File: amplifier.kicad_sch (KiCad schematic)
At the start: 16 parts, among them J1 Conn_01x01, J2 Conn_01x01, U2 IR2104, U5 IR2104

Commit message: Seems reasonable
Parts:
- removed C1, C9: C, symbol Device:C
- removed J1, J2: Conn_01x01, symbol Connector_Generic:Conn_01x01
- removed U10, U8: ~, symbol custom_symbols:NX3008N
- removed U2, U5: IR2104, Package_SO:SOIC-8_3.9x4.9mm_P1.27mm, symbol Driver_FET:IR2104
- added C11, C14, C15, C17, C4, C6: 10u, Capacitor_SMD:C_0603_1608Metric, symbol Device:C
- added Q1, Q2, Q3, Q4: DMN6140, Package_TO_SOT_SMD:SOT-23, symbol Transistor_FET:2N7002
- added R1, R11: 2k, Resistor_SMD:R_0603_1608Metric, symbol Device:R
- added TP2: LHI, TestPoint:TestPoint_Pad_D1.0mm, symbol Connector:TestPoint
- added TP4: LLO, TestPoint:TestPoint_Pad_D1.0mm, symbol Connector:TestPoint
- added TP6: RLO, TestPoint:TestPoint_Pad_D1.0mm, symbol Connector:TestPoint
- added TP7: RHI, TestPoint:TestPoint_Pad_D1.0mm, symbol Connector:TestPoint
- added U3: MIC4606, Package_SO:TSSOP-16-1EP_4.4x5mm_P0.65mm, symbol custom_symbols:MIC4606
- C10, C7, C8: value C -> 10u; footprint (none) -> Capacitor_SMD:C_0603_1608Metric
- R3, R5, R7, R9: value 100k -> 2k; footprint (none) -> Resistor_SMD:R_0603_1608Metric
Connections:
- net GND: now also C11.2, C14.2, C15.2, C17.2, C6.2, Q2.2 (S), Q4.2 (S), U3.13 (VSS)
- net OUT_A: now also C6.1, Q1.2 (S), Q2.3 (D), U3.15 (BHS); no longer C7.1, C8.1
- net OUT_B: now also C8.1, C4.2, Q3.2 (S), Q4.3 (D), U3.10 (AHS)
- net SIG_IN: now also R1.2
- net Vdrive: now also C7.1, C11.1, C14.1, Q1.3 (D), Q3.3 (D), U3.12 (VDD), U3.2 (EN); no longer C10.1
- net ~{SIG_IN}: now also R11.2
- net L_HI: now reaches R5.2
- net L_HI: now also TP2.1, U3.16 (BHO)
- net R_HI: now reaches R7.1
- net R_HI: now also TP7.1, U3.9 (AHO)
- net R_LO: now reaches R9.1
- net R_LO: now also TP6.1, U3.11 (ALO)
- net at R9.2: now also Q4.1 (G)
- net at R5.1: now also Q1.1 (G)
- net L_LO: now reaches R3.2
- net L_LO: now also TP4.1, U3.14 (BLO)
- net at R7.2: now also Q3.1 (G)
- net at R3.1: now also Q2.1 (G)
- new net: C10.1, U3.1 (BHB)
- new net: C17.1, R1.1, U3.3 (BPWM)
- new net: C15.1, R11.1, U3.6 (APWM)
- new net: C4.1, U3.8 (AHB)

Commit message: Tweaks
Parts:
- removed C6, C8: 10u, Capacitor_SMD:C_0603_1608Metric, symbol Device:C
- added C5: 2.2n, Capacitor_SMD:C_0603_1608Metric, symbol Device:C
- added L2: 10u, Inductor_SMD:L_1210_3225Metric, symbol Device:L
- C15, C17: value 10u -> 2.2n
- OUT1: now left out of the parts list
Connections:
- net GND: now also L2.2
- net OUT_A: now also C5.1
- new net: C5.2, L2.1
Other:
- moved on the sheet: TP2, TP4, TP6, TP7

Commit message: Tweaks
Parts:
- removed L2: 10u, Inductor_SMD:L_1210_3225Metric, symbol Device:L
- added C3: 220n, Capacitor_SMD:C_0603_1608Metric, symbol Device:C
- C15, C17: value 2.2n -> 1.5n
- C5: value 2.2n -> 220n
- TP2, TP4, TP6, TP7: now left out of the parts list
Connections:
- net GND: now also C5.2, C3.2
- net OUT_B: now also C3.1
- net Vdrive: no longer U3.2 (EN)
- new net EN: U3.2 (EN)
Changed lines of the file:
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@@
   (junction (at 114.3 57.15) (diameter 0) (color 0 0 0 0)
   )
+  (junction (at 137.16 68.58) (diameter 0) (color 0 0 0 0)
+  )
   (junction (at 43.18 107.95) (diameter 0) (color 0 0 0 0)
   )
-  (junction (at 59.69 92.71) (diameter 0) (color 0 0 0 0)
-  )
   (junction (at 114.3 68.58) (diameter 0) (color 0 0 0 0)
   )
@@
   (junction (at 102.87 90.17) (diameter 0) (color 0 0 0 0)
   )
+  (junction (at 137.16 90.17) (diameter 0) (color 0 0 0 0)
+  )
   (junction (at 55.88 92.71) (diameter 0) (color 0 0 0 0)
   )
@@
     (stroke (width 0) (type default))
   )
-  (wire (pts (xy 114.3 77.47) (xy 114.3 80.01))
-    (stroke (width 0) (type default))
-  )
   (wire (pts (xy 80.01 97.79) (xy 87.63 97.79))
     (stroke (width 0) (type default))
@@
     (stroke (width 0) (type default))
   )
-  (wire (pts (xy 114.3 87.63) (xy 114.3 90.17))
+  (wire (pts (xy 114.3 77.47) (xy 114.3 90.17))
     (stroke (width 0) (type default))
   )
@@
     (stroke (width 0) (type default))
   )
-  (wire (pts (xy 114.3 90.17) (xy 147.32 90.17))
+  (wire (pts (xy 114.3 90.17) (xy 137.16 90.17))
     (stroke (width 0) (type default))
   )
@@
     (stroke (width 0) (type default))
   )
-  (wire (pts (xy 59.69 102.87) (xy 59.69 92.71))
+  (wire (pts (xy 137.16 77.47) (xy 137.16 90.17))
     (stroke (width 0) (type default))
   )
@@
     (stroke (width 0) (type default))
   )
-  (wire (pts (xy 128.27 68.58) (xy 152.4 68.58))
+  (wire (pts (xy 128.27 68.58) (xy 137.16 68.58))
     (stroke (width 0) (type default))
   )
@@
     (stroke (width 0) (type default))
   )
+  (wire (pts (xy 137.16 90.17) (xy 147.32 90.17))
+    (stroke (width 0) (type default))
+  )
   (wire (pts (xy 80.01 90.17) (xy 80.01 92.71))
     (stroke (width 0) (type default))
@@
     (stroke (width 0) (type default))
   )
+  (wire (pts (xy 137.16 68.58) (xy 137.16 69.85))
+    (stroke (width 0) (type default))
+  )
   (wire (pts (xy 80.01 101.6) (xy 87.63 101.6))
     (stroke (width 0) (type default))
@@
     (stroke (width 0) (type default))
   )
-  (wire (pts (xy 59.69 92.71) (xy 63.5 92.71))
+  (wire (pts (xy 137.16 68.58) (xy 152.4 68.58))
     (stroke (width 0) (type default))
   )
@@
     (stroke (width 0) (type default))
   )
-  (wire (pts (xy 59.69 92.71) (xy 55.88 92.71))
+  (wire (pts (xy 55.88 92.71) (xy 63.5 92.71))
     (stroke (width 0) (type default))
   )
@@
   )
   (wire (pts (xy 152.4 69.85) (xy 152.4 68.58))
-    (stroke (width 0) (type default))
-  )
-  (wire (pts (xy 63.5 102.87) (xy 59.69 102.87))
     (stroke (width 0) (type default))
   )
@@
     (effects (font (size 1.27 1.27)) (justify left))
   )
+  (hierarchical_label "EN" (shape input) (at 63.5 102.87 180) (fields_autoplaced)
+    (effects (font (size 1.27 1.27)) (justify right))
+  )
   (symbol (lib_id "power:GND") (at 43.18 119.38 0) (unit 1)
     (in_bom yes) (on_board yes) (dnp no) (fields_autoplaced)
@@
         (path "/2e37f9ca-1f81-48a3-bbbb-9eab5c177622/9417e359-1c86-4e8d-97a7-eb92b3e0263a"
           (reference "#PWR07") (unit 1)
+        )
+      )
+    )
+  )
+  (symbol (lib_id "Device:C") (at 137.16 73.66 0) (unit 1)
+    (in_bom yes) (on_board yes) (dnp no)
+    (property "Reference" "C3" (at 138.43 71.12 0)
+      (effects (font (size 1.27 1.27)) (justify left))
+    )
+    (property "Value" "220n" (at 135.89 73.66 0)
+      (effects (font (size 1.27 1.27)) (justify left))
+    )
+    (property "Footprint" "Capacitor_SMD:C_0603_1608Metric" (at 138.1252 77.47 0)
+      (effects (font (size 1.27 1.27)) hide)
+    )
+    (property "Datasheet" "~" (at 137.16 73.66 0)
+      (effects (font (size 1.27 1.27)) hide)
+    )
+    (pin "1")
+    (pin "2")
+    (instances
+      (project "locator_beacon"
+        (path "/2e37f9ca-1f81-48a3-bbbb-9eab5c177622/9417e359-1c86-4e8d-97a7-eb92b3e0263a"
+          (reference "C3") (unit 1)
         )
       )
@@
   )
   (symbol (lib_id "Connector:TestPoint") (at 115.57 109.22 90) (unit 1)
-    (in_bom yes) (on_board yes) (dnp no)
+    (in_bom no) (on_board yes) (dnp no)
     (property "Reference" "TP4" (at 111.76 107.95 90)
       (effects (font (size 1.27 1.27)))
@@
   )
   (symbol (lib_id "Connector:TestPoint") (at 133.35 109.22 270) (unit 1)
-    (in_bom yes) (on_board yes) (dnp no)
+    (in_bom no) (on_board yes) (dnp no)
     (property "Reference" "TP6" (at 138.43 107.95 90)
       (effects (font (size 1.27 1.27)))
@@
   )
   (symbol (lib_id "Connector:TestPoint") (at 115.57 105.41 90) (unit 1)
-    (in_bom yes) (on_board yes) (dnp no)
+    (in_bom no) (on_board yes) (dnp no)
     (property "Reference" "TP2" (at 111.76 104.14 90)
       (effects (font (size 1.27 1.27)))
@@
   )
   (symbol (lib_id "Connector:TestPoint") (at 133.35 105.41 270) (unit 1)
-    (in_bom yes) (on_board yes) (dnp no)
+    (in_bom no) (on_board yes) (dnp no)
     (property "Reference" "TP7" (at 138.43 104.14 90)
       (effects (font (size 1.27 1.27)))
@@
       (effects (font (size 1.27 1.27)) (justify left))
     )
-    (property "Value" "2.2n" (at 113.03 73.66 0)
+    (property "Value" "220n" (at 113.03 73.66 0)
       (effects (font (size 1.27 1.27)) (justify left))
     )
@@
       (effects (font (size 1.27 1.27)) (justify left))
     )
-    (property "Value" "2.2n" (at 39.37 118.11 0)
+    (property "Value" "1.5n" (at 39.37 118.11 0)
       (effects (font (size 1.27 1.27)) (justify left))
     )
@@
       (effects (font (size 1.27 1.27)) (justify left))
     )
-    (property "Value" "2.2n" (at 46.99 104.14 0)
+    (property "Value" "1.5n" (at 46.99 104.14 0)
       (effects (font (size 1.27 1.27)) (justify left))
     )
@@
         )
       )
-    )
-  )
-  (symbol (lib_id "Device:L") (at 114.3 83.82 0) (unit 1)
-    (in_bom yes) (on_board yes) (dnp no) (fields_autoplaced)
-    (property "Reference" "L2" (at 115.57 82.55 0)
-      (effects (font (size 1.27 1.27)) (justify left))
-    )
-    (property "Value" "10u" (at 115.57 85.09 0)
-      (effects (font (size 1.27 1.27)) (justify left))
-    )
-    (property "Footprint" "Inductor_SMD:L_1210_3225Metric" (at 114.3 83.82 0)
-      (effects (font (size 1.27 1.27)) hide)
-    )
-    (property "Datasheet" "~" (at 114.3 83.82 0)
-      (effects (font (size 1.27 1.27)) hide)
-    )
-    (pin "1")
-    (pin "2")
-    (instances
-      (project "locator_beacon"
-        (path "/2e37f9ca-1f81-48a3-bbbb-9eab5c177622/9417e359-1c86-4e8d-97a7-eb92b3e0263a"
-          (reference "L2") (unit 1)
-        )
-      )

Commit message: changes
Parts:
- added C13, C16, C18, C19, C20, C6, C8, C9: 10u, Capacitor_SMD:C_0603_1608Metric, symbol Device:C
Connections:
- net GND: now also C13.2, C16.2, C18.2, C19.2, C20.2, C6.2, C8.2, C9.2
- net L_HI: no longer TP2.1
- net L_LO: no longer TP4.1
- net R_HI: no longer TP7.1
- net R_LO: no longer TP6.1
- net Vdrive: now also C13.1, C16.1, C18.1, C19.1, C20.1, C6.1, C8.1, C9.1
- net at Q3.1 (G), R7.2: now also TP7.1
- net at Q1.1 (G), R5.1: now also TP2.1
- net at Q4.1 (G), R9.2: now also TP6.1
- net at Q2.1 (G), R3.1: now also TP4.1
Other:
- note added: "what do you mean unnecessary?"
- moved on the sheet: C11, C14, TP2, TP4, TP6, TP7

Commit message: Shrunkified
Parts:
- removed C6, C8: 10u, Capacitor_SMD:C_0603_1608Metric, symbol Device:C
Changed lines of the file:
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@@
   (junction (at 137.16 68.58) (diameter 0) (color 0 0 0 0)
   )
-  (junction (at 33.02 60.96) (diameter 0) (color 0 0 0 0)
-  )
   (junction (at 63.5 60.96) (diameter 0) (color 0 0 0 0)
   )
@@
   (junction (at 43.18 107.95) (diameter 0) (color 0 0 0 0)
   )
-  (junction (at 48.26 60.96) (diameter 0) (color 0 0 0 0)
-  )
   (junction (at 114.3 68.58) (diameter 0) (color 0 0 0 0)
   )
@@
   (junction (at 55.88 111.76) (diameter 0) (color 0 0 0 0)
   )
-  (junction (at 33.02 53.34) (diameter 0) (color 0 0 0 0)
-  )
   (junction (at 58.42 60.96) (diameter 0) (color 0 0 0 0)
   )
-  (junction (at 48.26 53.34) (diameter 0) (color 0 0 0 0)
-  )
   (junction (at 91.44 74.93) (diameter 0) (color 0 0 0 0)
   )
@@
     (stroke (width 0) (type default))
   )
-  (wire (pts (xy 27.94 53.34) (xy 33.02 53.34))
-    (stroke (width 0) (type default))
-  )
-  (wire (pts (xy 48.26 53.34) (xy 53.34 53.34))
+  (wire (pts (xy 27.94 53.34) (xy 38.1 53.34))
     (stroke (width 0) (type default))
   )
@@
     (stroke (width 0) (type default))
   )
-  (wire (pts (xy 43.18 53.34) (xy 48.26 53.34))
+  (wire (pts (xy 43.18 53.34) (xy 53.34 53.34))
     (stroke (width 0) (type default))
   )
@@
     (stroke (width 0) (type default))
   )
-  (wire (pts (xy 43.18 60.96) (xy 48.26 60.96))
-    (stroke (width 0) (type default))
-  )
-  (wire (pts (xy 48.26 60.96) (xy 53.34 60.96))
+  (wire (pts (xy 43.18 60.96) (xy 53.34 60.96))
     (stroke (width 0) (type default))
   )
@@
     (stroke (width 0) (type default))
   )
-  (wire (pts (xy 33.02 60.96) (xy 38.1 60.96))
+  (wire (pts (xy 27.94 60.96) (xy 38.1 60.96))
     (stroke (width 0) (type default))
   )
@@
     (stroke (width 0) (type default))
   )
-  (wire (pts (xy 27.94 60.96) (xy 33.02 60.96))
-    (stroke (width 0) (type default))
-  )
   (wire (pts (xy 43.18 111.76) (xy 43.18 107.95))
     (stroke (width 0) (type default))
@@
   )
   (wire (pts (xy 152.4 67.31) (xy 152.4 68.58))
-    (stroke (width 0) (type default))
-  )
-  (wire (pts (xy 33.02 53.34) (xy 38.1 53.34))
     (stroke (width 0) (type default))
   )
@@
         (path "/2e37f9ca-1f81-48a3-bbbb-9eab5c177622/9417e359-1c86-4e8d-97a7-eb92b3e0263a"
           (reference "C20") (unit 1)
-        )
-      )
-    )
-  )
-  (symbol (lib_id "Device:C") (at 48.26 57.15 0) (unit 1)
-    (in_bom yes) (on_board yes) (dnp no)
-    (property "Reference" "C8" (at 48.26 54.61 0)
-      (effects (font (size 1.27 1.27)) (justify left))
-    )
-    (property "Value" "10u" (at 46.99 57.15 0)
-      (effects (font (size 1.27 1.27)) (justify left))
-    )
-    (property "Footprint" "Capacitor_SMD:C_0603_1608Metric" (at 49.2252 60.96 0)
-      (effects (font (size 1.27 1.27)) hide)
-    )
-    (property "Datasheet" "~" (at 48.26 57.15 0)
-      (effects (font (size 1.27 1.27)) hide)
-    )
-    (pin "1")
-    (pin "2")
-    (instances
-      (project "locator_beacon"
-        (path "/2e37f9ca-1f81-48a3-bbbb-9eab5c177622/9417e359-1c86-4e8d-97a7-eb92b3e0263a"
-          (reference "C8") (unit 1)
         )
       )
@@
         )
       )
-    )
-  )
-  (symbol (lib_id "Device:C") (at 33.02 57.15 0) (unit 1)
-    (in_bom yes) (on_board yes) (dnp no)
-    (property "Reference" "C6" (at 33.02 54.61 0)
-      (effects (font (size 1.27 1.27)) (justify left))
-    )
-    (property "Value" "10u" (at 31.75 57.15 0)
-      (effects (font (size 1.27 1.27)) (justify left))
-    )
-    (property "Footprint" "Capacitor_SMD:C_0603_1608Metric" (at 33.9852 60.96 0)
-      (effects (font (size 1.27 1.27)) hide)
-    )
-    (property "Datasheet" "~" (at 33.02 57.15 0)
-      (effects (font (size 1.27 1.27)) hide)
-    )
-    (pin "1")
-    (pin "2")
-    (instances
-      (project "locator_beacon"
-        (path "/2e37f9ca-1f81-48a3-bbbb-9eab5c177622/9417e359-1c86-4e8d-97a7-eb92b3e0263a"
-          (reference "C6") (unit 1)
-        )
-      )

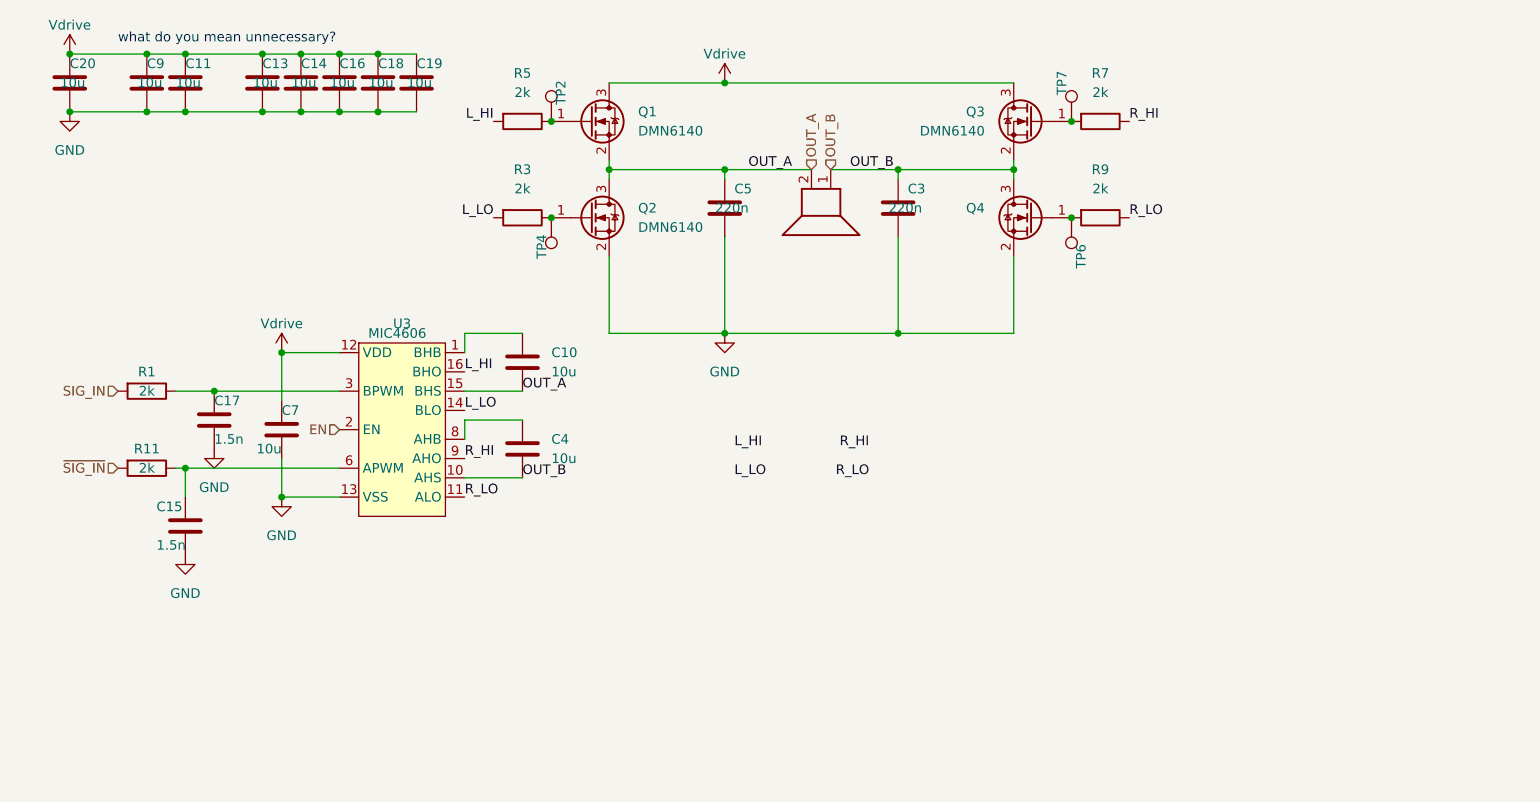
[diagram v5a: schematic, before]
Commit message: Separate +12 and boost
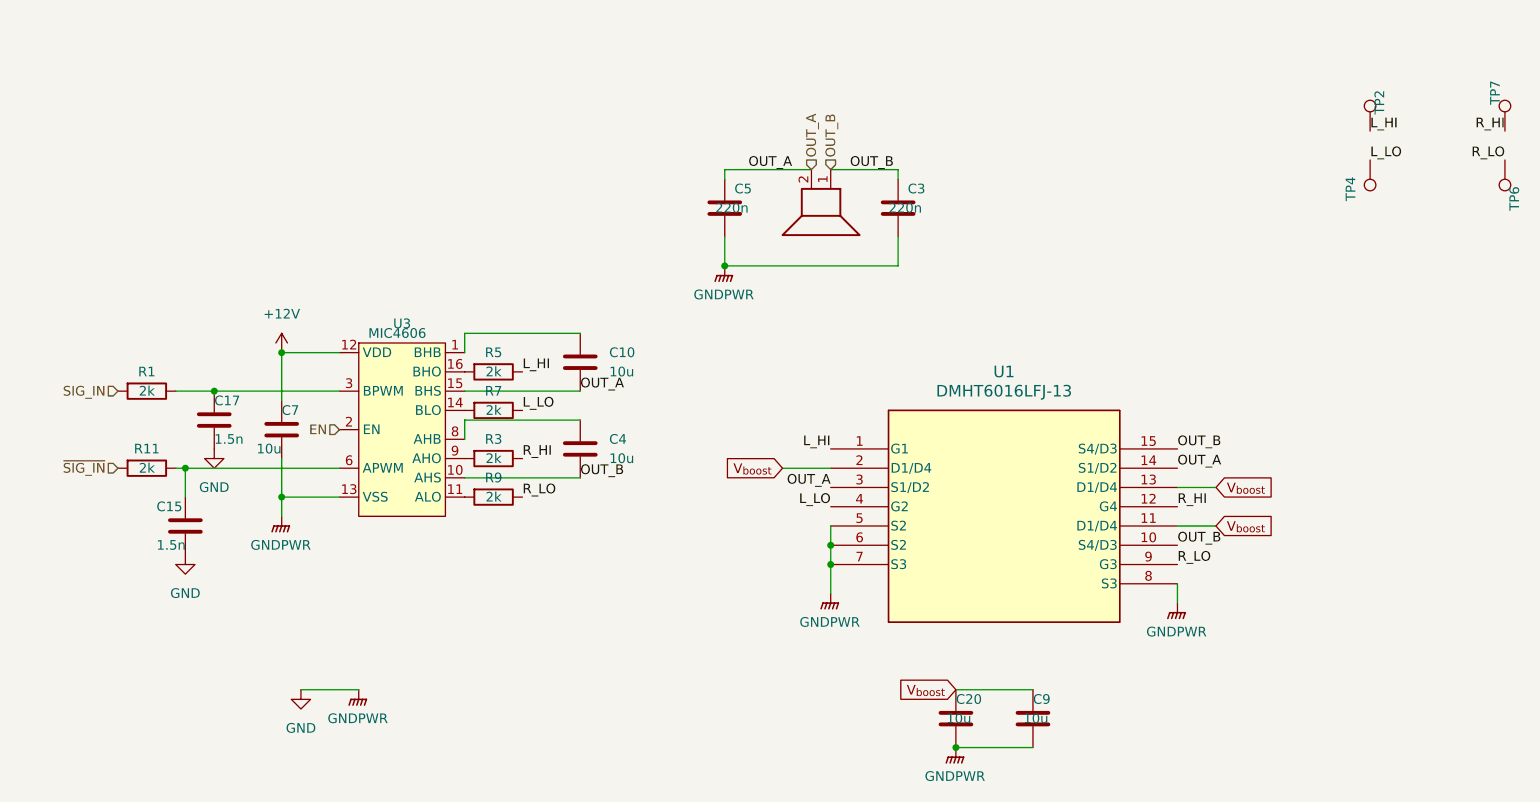
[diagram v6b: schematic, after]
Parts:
- removed C11, C13, C14, C16, C18, C19: 10u, Capacitor_SMD:C_0603_1608Metric, symbol Device:C
- removed Q1, Q2, Q3, Q4: DMN6140, Package_TO_SOT_SMD:SOT-23, symbol Transistor_FET:2N7002
- added U1: DMHT6016LFJ-13, custom:V-DFN5045-12_DIO, symbol custom_symbols:DMHT6016LFJ-13
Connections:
- net GND: now also U1.5 (S2), U1.6 (S2), U1.7 (S3), U1.8 (S3)
- net L_HI: now also R5.1, TP2.1, U1.1 (G1); no longer R5.2, U3.16 (BHO)
- net L_LO: now also R7.1, TP4.1, U1.4 (G2); no longer R3.2, U3.14 (BLO)
- net OUT_A: now also U1.14 (S1/D2), U1.3 (S1/D2)
- net OUT_B: now also U1.10 (S4/D3), U1.15 (S4/D3)
- net R_HI: now also R3.1, TP7.1, U1.12 (G4); no longer R7.1, U3.9 (AHO)
- net R_LO: now also TP6.1, U1.9 (G3); no longer U3.11 (ALO)
- net at R7.2: now also U3.14 (BLO); no longer TP7.1
- net at R9.2: now also U3.11 (ALO); no longer TP6.1
- net Vdrive renamed +12V
- net +12V: no longer C20.1, C9.1
- new net: R5.2, U3.16 (BHO)
- new net: R3.2, U3.9 (AHO)
- new net V_{boost}: C20.1, C9.1, U1.11 (D1/D4), U1.13 (D1/D4), U1.2 (D1/D4)
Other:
- note removed: "what do you mean unnecessary?"
- moved on the sheet: C10, C20, C4, C9, R3, R5, R7, R9, TP2, TP4, TP6, TP7
